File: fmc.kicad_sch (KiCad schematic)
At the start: 6 parts, among them P1 ASP-134604-01, P2 ASP-134604-01

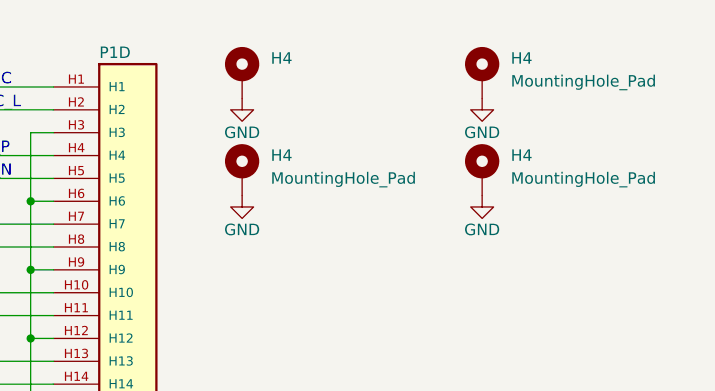
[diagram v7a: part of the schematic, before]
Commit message: Finalized Design & Board
Change to design
-Added resistor options to choose the grounding of input connectors
-uploaded libraries
-uploaded generated BOM
- adjusted mounting holes on front of board by 10mil
-Changed input AC blocking cap to 10nF from 100nF due to part availability
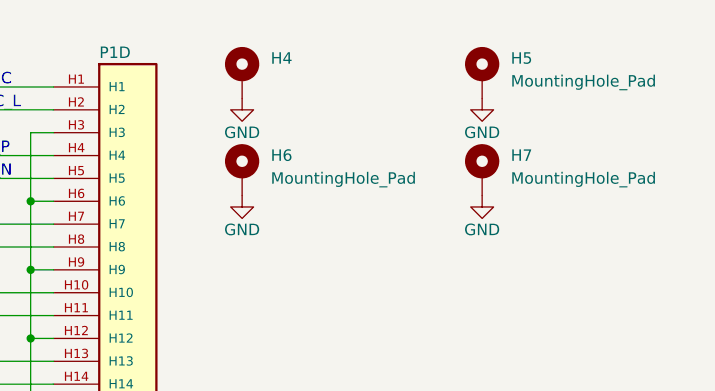
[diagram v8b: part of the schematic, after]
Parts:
- H4: footprint footprints:Mounting Hole 3mm hole 5mm ring -> QuartzFootprints:Mounting Hole 3mm hole 5mm ring; now left out of the parts list
- H5, H6, H7: renamed from H4; footprint footprints:Mounting Hole 3mm hole 5mm ring -> QuartzFootprints:Mounting Hole 3mm hole 5mm ring; now left out of the parts list
- P1, P2: footprint AD7768_Digitizer:SAMTEC_ASP-134604-01 -> QuartzFootprints:SAMTEC_ASP-134604-01
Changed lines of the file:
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@@
       (effects (font (size 1.27 1.27)) (justify left))
     )
-    (property "Footprint" "AD7768_Digitizer:SAMTEC_ASP-134604-01" (at 41.91 259.08 0)
+    (property "Footprint" "QuartzFootprints:SAMTEC_ASP-134604-01" (at 41.91 259.08 0)
       (effects (font (size 1.27 1.27)) (justify bottom) hide)
     )
@@
   )
   (symbol (lib_id "Mechanical:MountingHole_Pad") (at 365.125 31.115 0) (unit 1)
-    (in_bom yes) (on_board yes) (dnp no) (fields_autoplaced)
-    (property "Reference" "H4" (at 368.3 29.21 0)
+    (in_bom no) (on_board yes) (dnp no) (fields_autoplaced)
+    (property "Reference" "H7" (at 368.3 29.21 0)
       (effects (font (size 1.27 1.27)) (justify left))
     )
@@
       (effects (font (size 1.27 1.27)) (justify left))
     )
-    (property "Footprint" "footprints:Mounting Hole 3mm hole 5mm ring" (at 365.125 31.115 0)
+    (property "Footprint" "QuartzFootprints:Mounting Hole 3mm hole 5mm ring" (at 365.125 31.115 0)
       (effects (font (size 1.27 1.27)) hide)
     )
@@
     (instances
       (project "Quartz_v1p1"
-        (path "/674e1e7f-67ba-4e85-a926-dcd5f6a22021"
-          (reference "H4") (unit 1)
-        )
         (path "/674e1e7f-67ba-4e85-a926-dcd5f6a22021/9fe24aff-0307-4354-b185-f0174f24220c"
           (reference "H7") (unit 1)
@@
   )
   (symbol (lib_id "Mechanical:MountingHole_Pad") (at 365.125 20.32 0) (unit 1)
-    (in_bom yes) (on_board yes) (dnp no) (fields_autoplaced)
-    (property "Reference" "H4" (at 368.3 18.415 0)
+    (in_bom no) (on_board yes) (dnp no) (fields_autoplaced)
+    (property "Reference" "H5" (at 368.3 18.415 0)
       (effects (font (size 1.27 1.27)) (justify left))
     )
@@
       (effects (font (size 1.27 1.27)) (justify left))
     )
-    (property "Footprint" "footprints:Mounting Hole 3mm hole 5mm ring" (at 365.125 20.32 0)
+    (property "Footprint" "QuartzFootprints:Mounting Hole 3mm hole 5mm ring" (at 365.125 20.32 0)
       (effects (font (size 1.27 1.27)) hide)
     )
@@
     (instances
       (project "Quartz_v1p1"
-        (path "/674e1e7f-67ba-4e85-a926-dcd5f6a22021"
-          (reference "H4") (unit 1)
-        )
         (path "/674e1e7f-67ba-4e85-a926-dcd5f6a22021/9fe24aff-0307-4354-b185-f0174f24220c"
           (reference "H5") (unit 1)
@@
       (effects (font (size 1.27 1.27)) (justify left))
     )
-    (property "Footprint" "AD7768_Digitizer:SAMTEC_ASP-134604-01" (at 41.91 139.7 0)
+    (property "Footprint" "QuartzFootprints:SAMTEC_ASP-134604-01" (at 41.91 139.7 0)
       (effects (font (size 1.27 1.27)) (justify bottom) hide)
     )
@@
   )
   (symbol (lib_id "Mechanical:MountingHole_Pad") (at 338.455 20.32 0) (unit 1)
-    (in_bom yes) (on_board yes) (dnp no) (fields_autoplaced)
+    (in_bom no) (on_board yes) (dnp no) (fields_autoplaced)
     (property "Reference" "H4" (at 341.63 18.415 0)
       (effects (font (size 1.27 1.27)) (justify left))
@@
       (effects (font (size 1.27 1.27)) (justify left) hide)
     )
-    (property "Footprint" "footprints:Mounting Hole 3mm hole 5mm ring" (at 338.455 20.32 0)
+    (property "Footprint" "QuartzFootprints:Mounting Hole 3mm hole 5mm ring" (at 338.455 20.32 0)
       (effects (font (size 1.27 1.27)) hide)
     )
@@
     (instances
       (project "Quartz_v1p1"
-        (path "/674e1e7f-67ba-4e85-a926-dcd5f6a22021"
-          (reference "H4") (unit 1)
-        )
         (path "/674e1e7f-67ba-4e85-a926-dcd5f6a22021/9fe24aff-0307-4354-b185-f0174f24220c"
           (reference "H4") (unit 1)
@@
       (effects (font (size 1.27 1.27)) (justify left) hide)
     )
-    (property "Footprint" "AD7768_Digitizer:SAMTEC_ASP-134604-01" (at 180.34 260.35 0)
+    (property "Footprint" "QuartzFootprints:SAMTEC_ASP-134604-01" (at 180.34 260.35 0)
       (effects (font (size 1.27 1.27)) (justify bottom) hide)
     )
@@
       (effects (font (size 1.27 1.27)) (justify left) hide)
     )
-    (property "Footprint" "AD7768_Digitizer:SAMTEC_ASP-134604-01" (at 111.76 139.7 0)
+    (property "Footprint" "QuartzFootprints:SAMTEC_ASP-134604-01" (at 111.76 139.7 0)
       (effects (font (size 1.27 1.27)) (justify bottom) hide)
     )
@@
       (effects (font (size 1.27 1.27)) (justify left) hide)
     )
-    (property "Footprint" "AD7768_Digitizer:SAMTEC_ASP-134604-01" (at 111.76 260.35 0)
+    (property "Footprint" "QuartzFootprints:SAMTEC_ASP-134604-01" (at 111.76 260.35 0)
       (effects (font (size 1.27 1.27)) (justify bottom) hide)
     )
@@
       (effects (font (size 1.27 1.27)) (justify left) hide)
     )
-    (property "Footprint" "AD7768_Digitizer:SAMTEC_ASP-134604-01" (at 180.34 139.7 0)
+    (property "Footprint" "QuartzFootprints:SAMTEC_ASP-134604-01" (at 180.34 139.7 0)
       (effects (font (size 1.27 1.27)) (justify bottom) hide)
     )
@@
       (effects (font (size 1.27 1.27)) (justify left) hide)
     )
-    (property "Footprint" "AD7768_Digitizer:SAMTEC_ASP-134604-01" (at 247.65 261.62 0)
+    (property "Footprint" "QuartzFootprints:SAMTEC_ASP-134604-01" (at 247.65 261.62 0)
       (effects (font (size 1.27 1.27)) (justify bottom) hide)
     )
@@
   )
   (symbol (lib_id "Mechanical:MountingHole_Pad") (at 338.455 31.115 0) (unit 1)
-    (in_bom yes) (on_board yes) (dnp no) (fields_autoplaced)
-    (property "Reference" "H4" (at 341.63 29.21 0)
+    (in_bom no) (on_board yes) (dnp no) (fields_autoplaced)
+    (property "Reference" "H6" (at 341.63 29.21 0)
       (effects (font (size 1.27 1.27)) (justify left))
     )
@@
       (effects (font (size 1.27 1.27)) (justify left))
     )
-    (property "Footprint" "footprints:Mounting Hole 3mm hole 5mm ring" (at 338.455 31.115 0)
+    (property "Footprint" "QuartzFootprints:Mounting Hole 3mm hole 5mm ring" (at 338.455 31.115 0)
       (effects (font (size 1.27 1.27)) hide)
     )
@@
     (instances
       (project "Quartz_v1p1"
-        (path "/674e1e7f-67ba-4e85-a926-dcd5f6a22021"
-          (reference "H4") (unit 1)
-        )
         (path "/674e1e7f-67ba-4e85-a926-dcd5f6a22021/9fe24aff-0307-4354-b185-f0174f24220c"
           (reference "H6") (unit 1)
@@
       (effects (font (size 1.27 1.27)) (justify left) hide)
     )
-    (property "Footprint" "AD7768_Digitizer:SAMTEC_ASP-134604-01" (at 247.65 139.7 0)
+    (property "Footprint" "QuartzFootprints:SAMTEC_ASP-134604-01" (at 247.65 139.7 0)
       (effects (font (size 1.27 1.27)) (justify bottom) hide)
     )
